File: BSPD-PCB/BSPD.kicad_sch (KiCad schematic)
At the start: 79 parts, among them J1 Conn_01x03_Socket, J2 Conn_01x03_Socket, J3 Conn_01x02_Socket, J4 Conn_01x02_Socket, K1 Relay_SPST-NO, Q1 2N7002, Q2 2N7002, U1 LM393, U2 LM393, U3 TPS7B88-Q1, U4 74LVC1G11, U5 74LVC1G332, U6 LTC6994xS6-1, U7 LTC6994xS6-1, U8 74LVC1G332

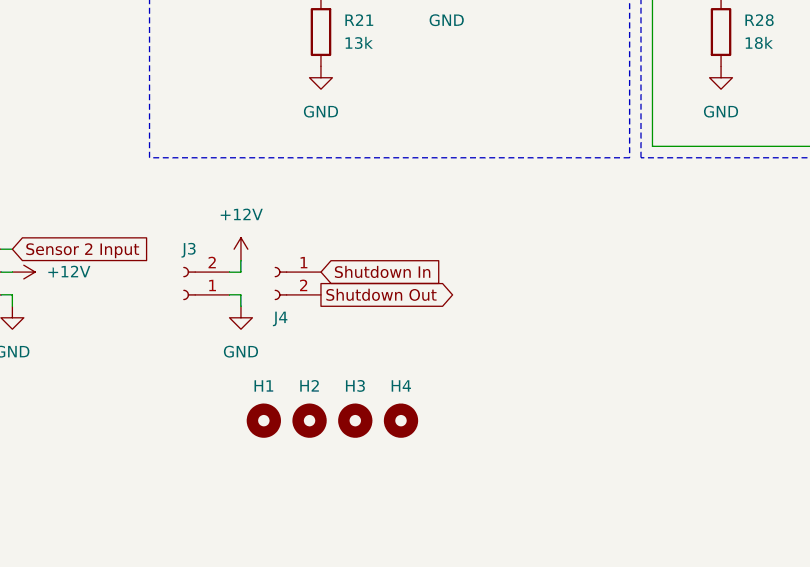
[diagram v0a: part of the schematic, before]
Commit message: Updated production gerbers
Reversed shutdown connector
Added back test points 1 and 2
Fixed shutdown connector placement
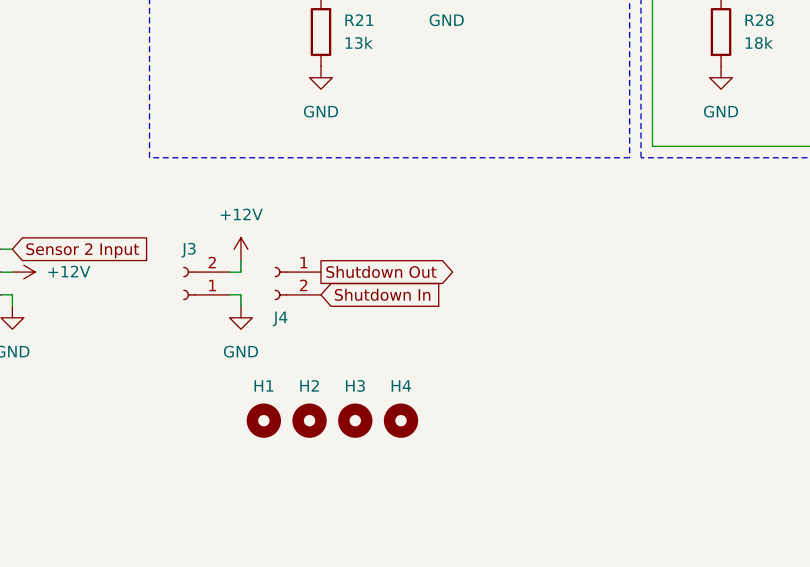
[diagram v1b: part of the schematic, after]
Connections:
- net Shutdown In: now also J4.2 (Pin_2); no longer J4.1 (Pin_1)
- net Shutdown Out: now also J4.1 (Pin_1); no longer J4.2 (Pin_2)
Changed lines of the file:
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@@
 	(global_label "Shutdown Out"
 		(shape output)
-		(at 158.75 179.07 0)
+		(at 158.75 176.53 0)
 		(fields_autoplaced yes)
 		(effects
@@
 		)
 		(property "Intersheetrefs" "${INTERSHEET_REFS}"
-			(at 174.9187 179.07 0)
+			(at 174.9187 176.53 0)
 			(effects
 				(font
@@
 	(global_label "Shutdown In"
 		(shape input)
-		(at 158.75 176.53 0)
+		(at 158.75 179.07 0)
 		(fields_autoplaced yes)
 		(effects
@@
 		)
 		(property "Intersheetrefs" "${INTERSHEET_REFS}"
-			(at 173.4673 176.53 0)
+			(at 173.4673 179.07 0)
 			(effects
 				(font

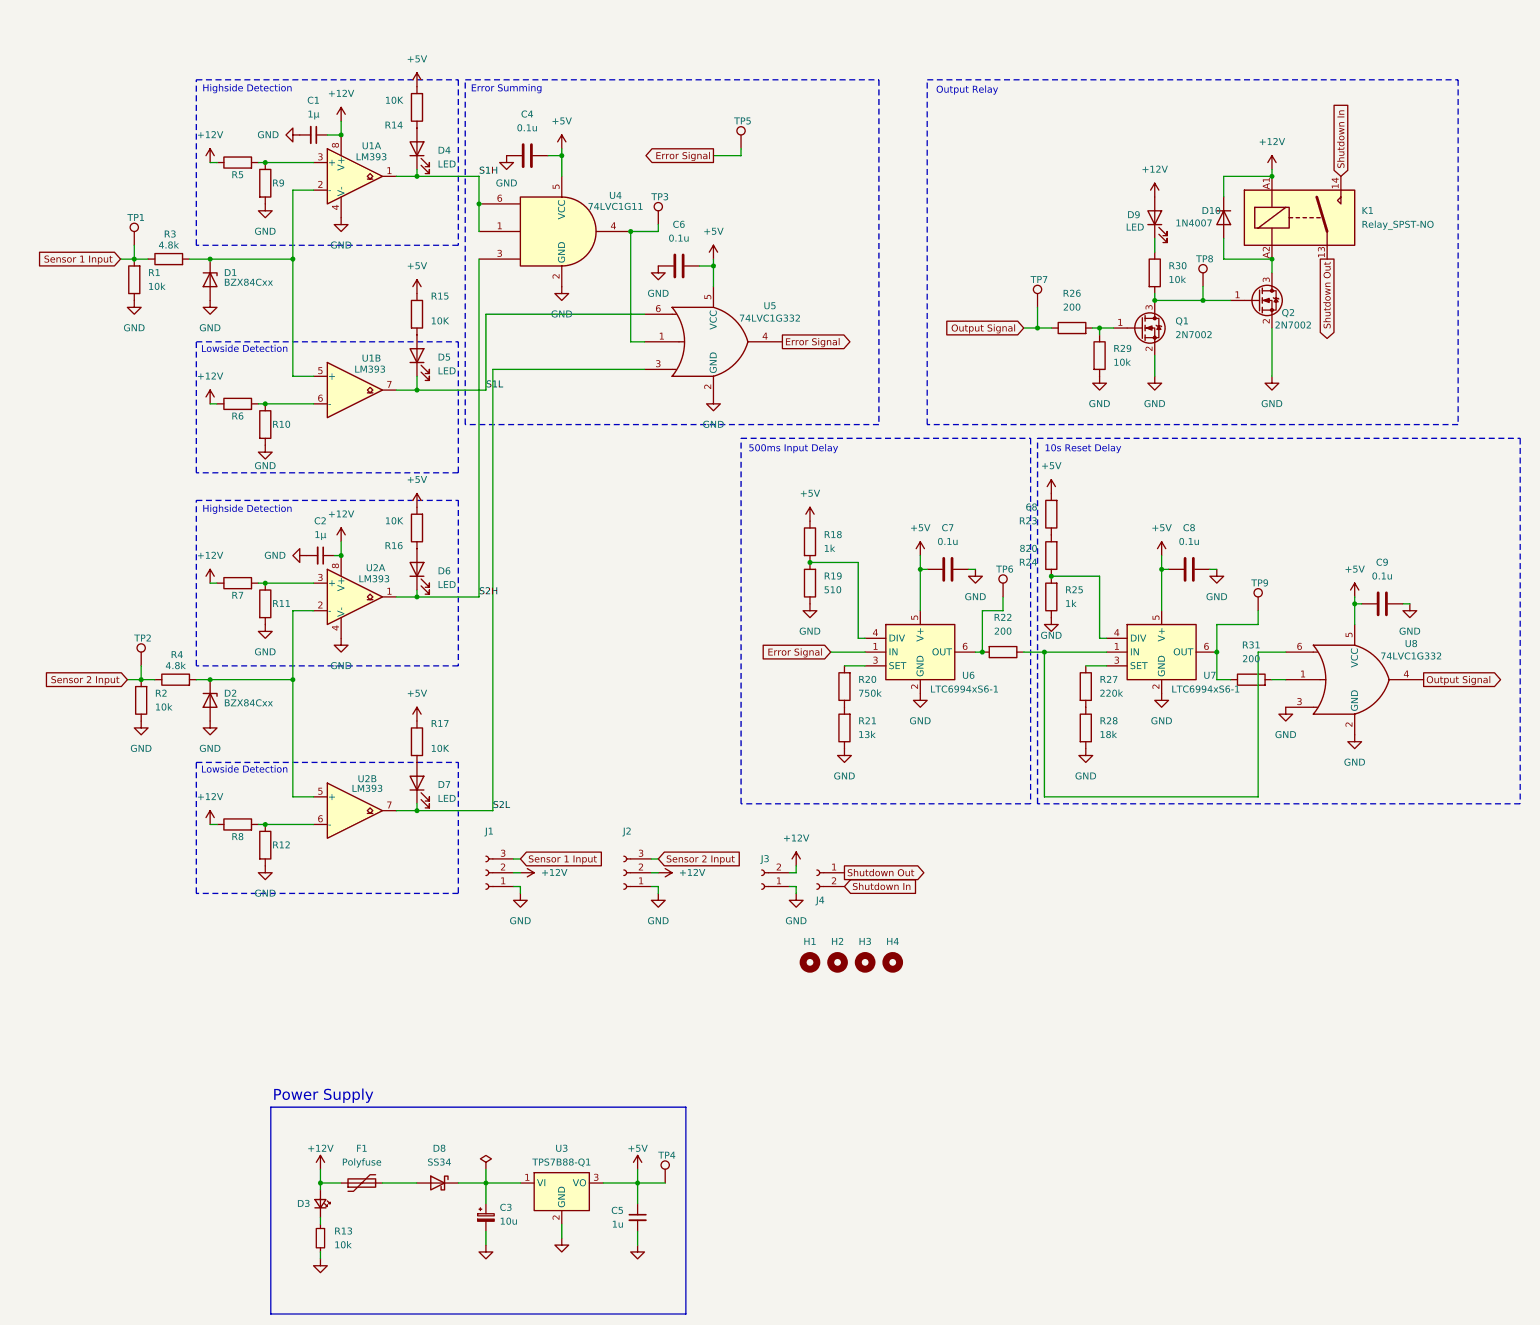
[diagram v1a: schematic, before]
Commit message: V1.4
Replaced Comparators for push pull (not yet selected)
Changed input block to 5V
Added more test points
Changed Zener Package
Moved Diodes to active high
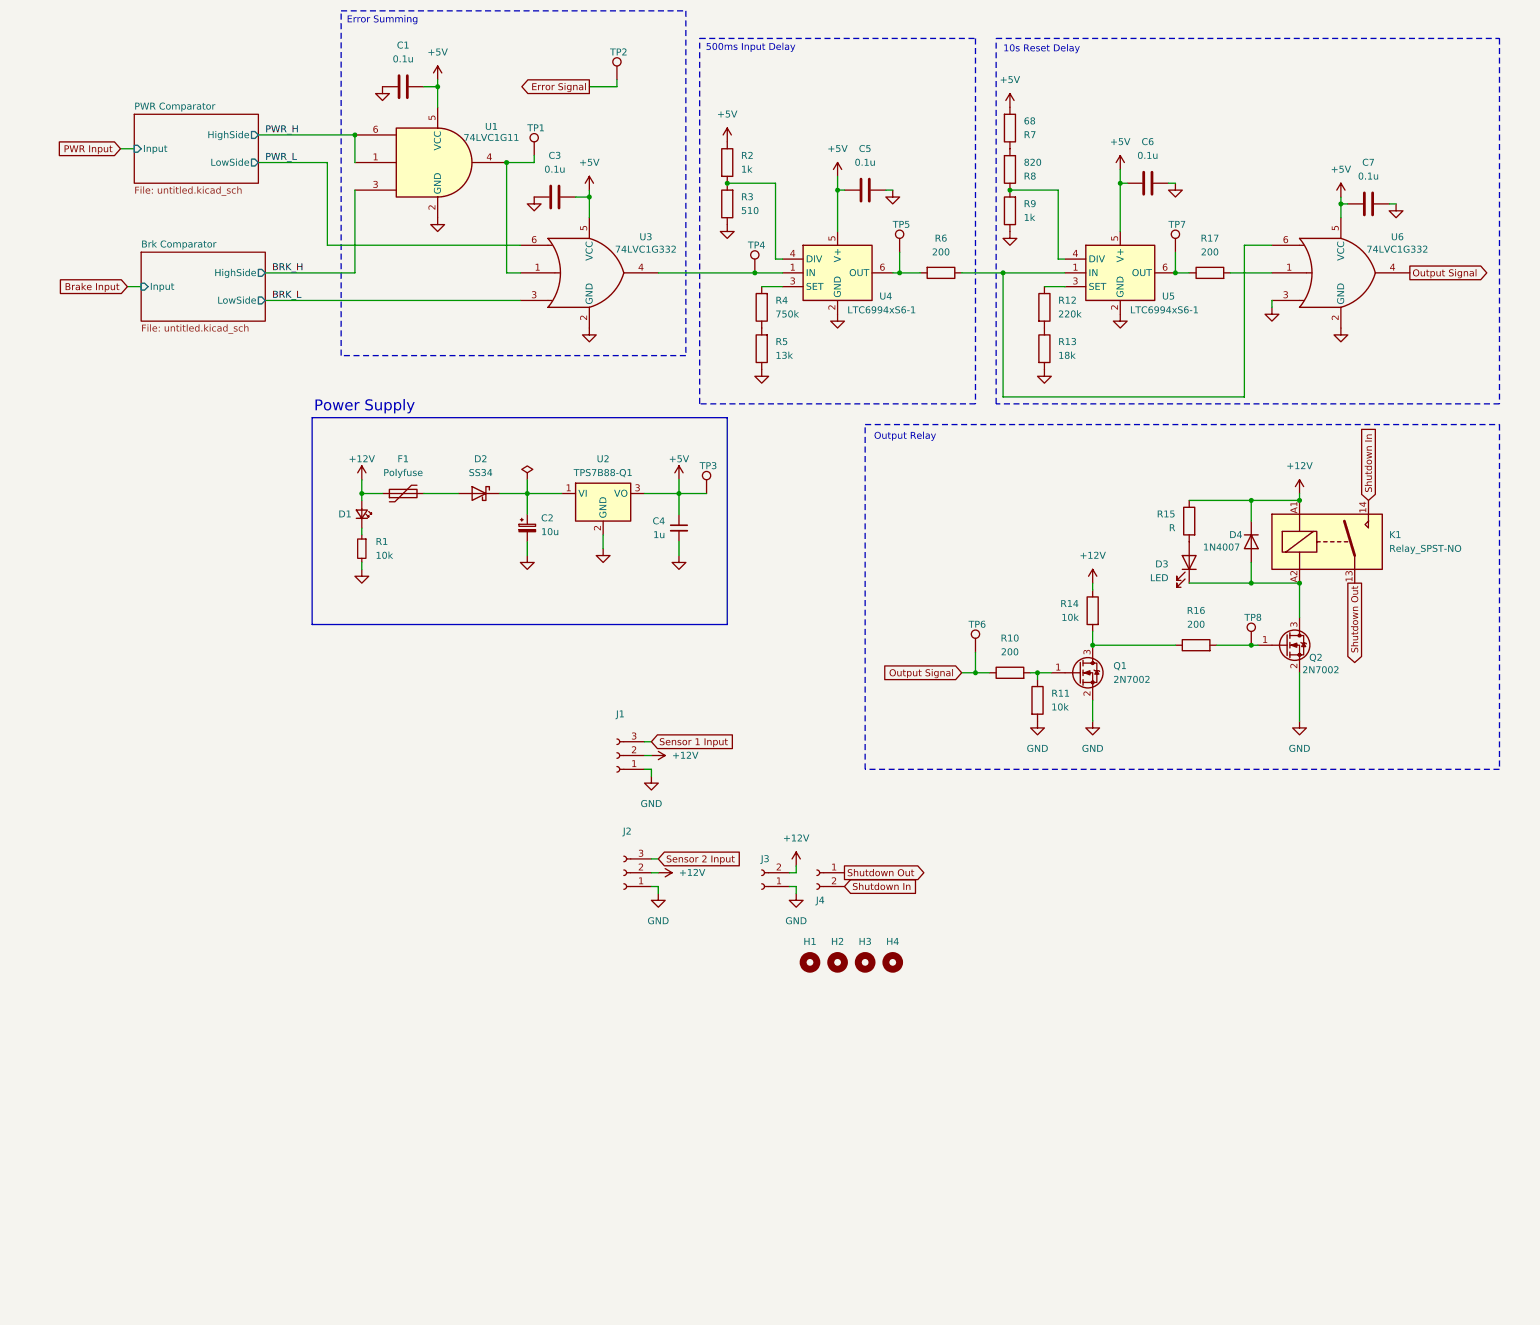
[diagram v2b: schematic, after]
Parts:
- removed C1, C2: 1µ, Capacitor_SMD:C_0603_1608Metric, symbol Device:C_Small
- removed D1, D2: BZX84Cxx, Package_TO_SOT_SMD:SOT-23, symbol Diode:BZX84Cxx
- removed D4, D5, D6, D7, D9: LED, LED_SMD:LED_0603_1608Metric, symbol Device:LED
- removed R1, R2: 10k, Resistor_SMD:R_0603_1608Metric, symbol Device:R
- removed R10, R11, R12, R9: 62k, Resistor_SMD:R_0603_1608Metric, symbol Device:R
- removed R14, R17: 10K, Resistor_SMD:R_0603_1608Metric, symbol Device:R
- removed R3, R4: 4.8k, Resistor_SMD:R_0603_1608Metric, symbol Device:R
- removed R5, R6, R7, R8: 39K, Resistor_SMD:R_0603_1608Metric, symbol Device:R
- removed TP1, TP2: TestPoint, TestPoint:TestPoint_Keystone_5000-5004_Miniature, symbol Connector:TestPoint
- removed U1, U2: LM393, Package_SO:SOIC-8_3.9x4.9mm_P1.27mm, symbol Comparator:LM393
- added D3: LED, LED_SMD:LED_0603_1608Metric, symbol Device:LED
- added TP4: TestPoint, TestPoint:TestPoint_Keystone_5000-5004_Miniature, symbol Connector:TestPoint
- R15: value 10K -> R
- R16: value 10K -> 200
- renumbered C4 to C1, C3 to C2, C6 to C3, C5 to C4, C7 to C5, C8 to C6, C9 to C7, D3 to D1, D8 to D2, D10 to D4, R13 to R1, R26 to R10, R29 to R11, R27 to R12, R28 to R13, R30 to R14, R31 to R17, R18 to R2, R19 to R3, R20 to R4, R21 to R5, R22 to R6, R23 to R7, R24 to R8, R25 to R9, TP3 to TP1, TP5 to TP2, TP4 to TP3, TP6 to TP5, TP7 to TP6, TP9 to TP7, U4 to U1, U3 to U2, U5 to U3, U6 to U4, U7 to U5, U8 to U6
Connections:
- net +12V: now also R14.1, R15.1
- net +5V: no longer R15.1, R16.2
- net Error Signal: no longer U3.4, U4.1 (IN)
- net at Q1.3 (D), R14.2: now also R16.1; no longer Q2.1 (G), TP8.1
- net at D4.2 (A), K1.A2, Q2.3 (D): now also D3.1 (K)
- net at R15.2: now also D3.2 (A)
- net S1H renamed PWR_H
- net S1L renamed PWR_L
- net S2H renamed BRK_H
- net S2L renamed BRK_L
- new net: Q2.1 (G), R16.2, TP8.1
- new net: TP4.1, U3.4, U4.1 (IN)
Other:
- added sheet Brk Comparator (untitled.kicad_sch)
- added sheet PWR Comparator (untitled.kicad_sch)
- note removed: "Highside Detection"
- note removed: "Lowside Detection"
- moved on the sheet: C1, C2, C3, C4, C5, C6, C7, D1, D2, D4, F1, J1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
